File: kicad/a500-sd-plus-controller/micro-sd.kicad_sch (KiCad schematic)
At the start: 19 parts, among them J1 Micro_SD_Card_Det2, J3 Micro_SD_Card_Det2, U10 RT9013-33, U5 SRV05-4, U8 RT9013-33

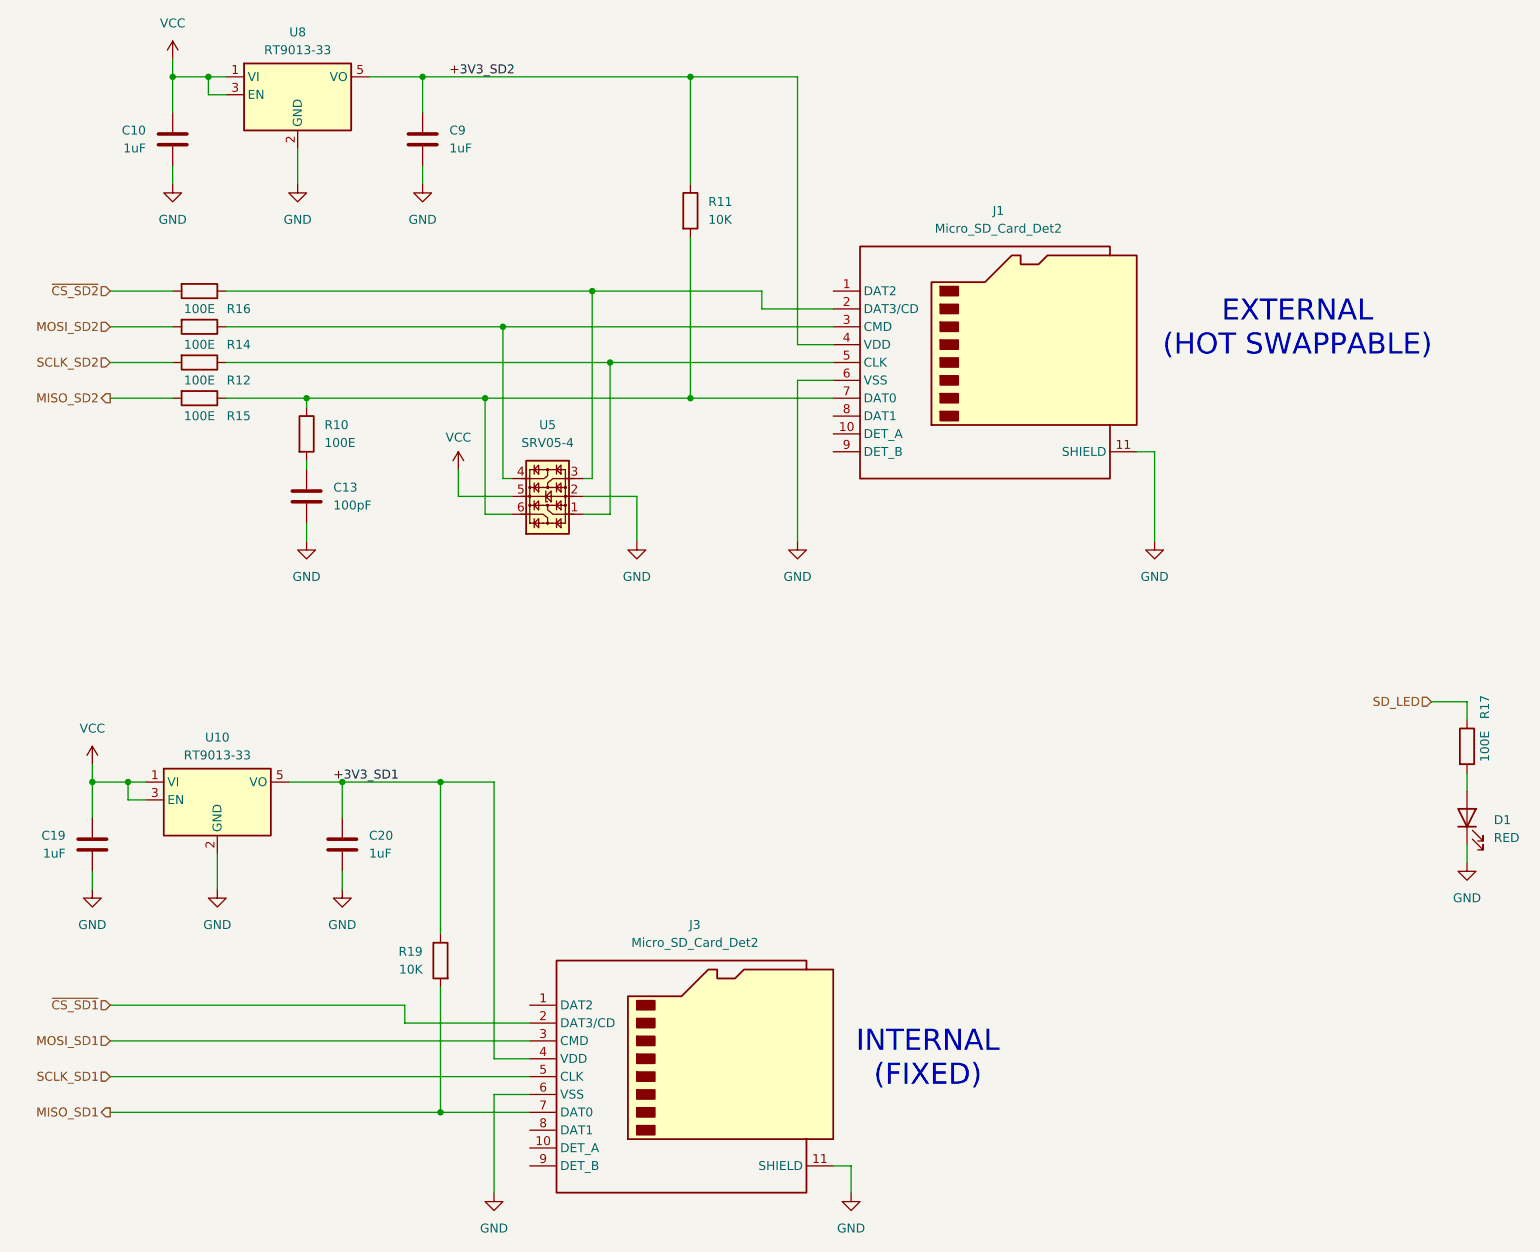
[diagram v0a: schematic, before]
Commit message: added add ethernet controller
still work in progress
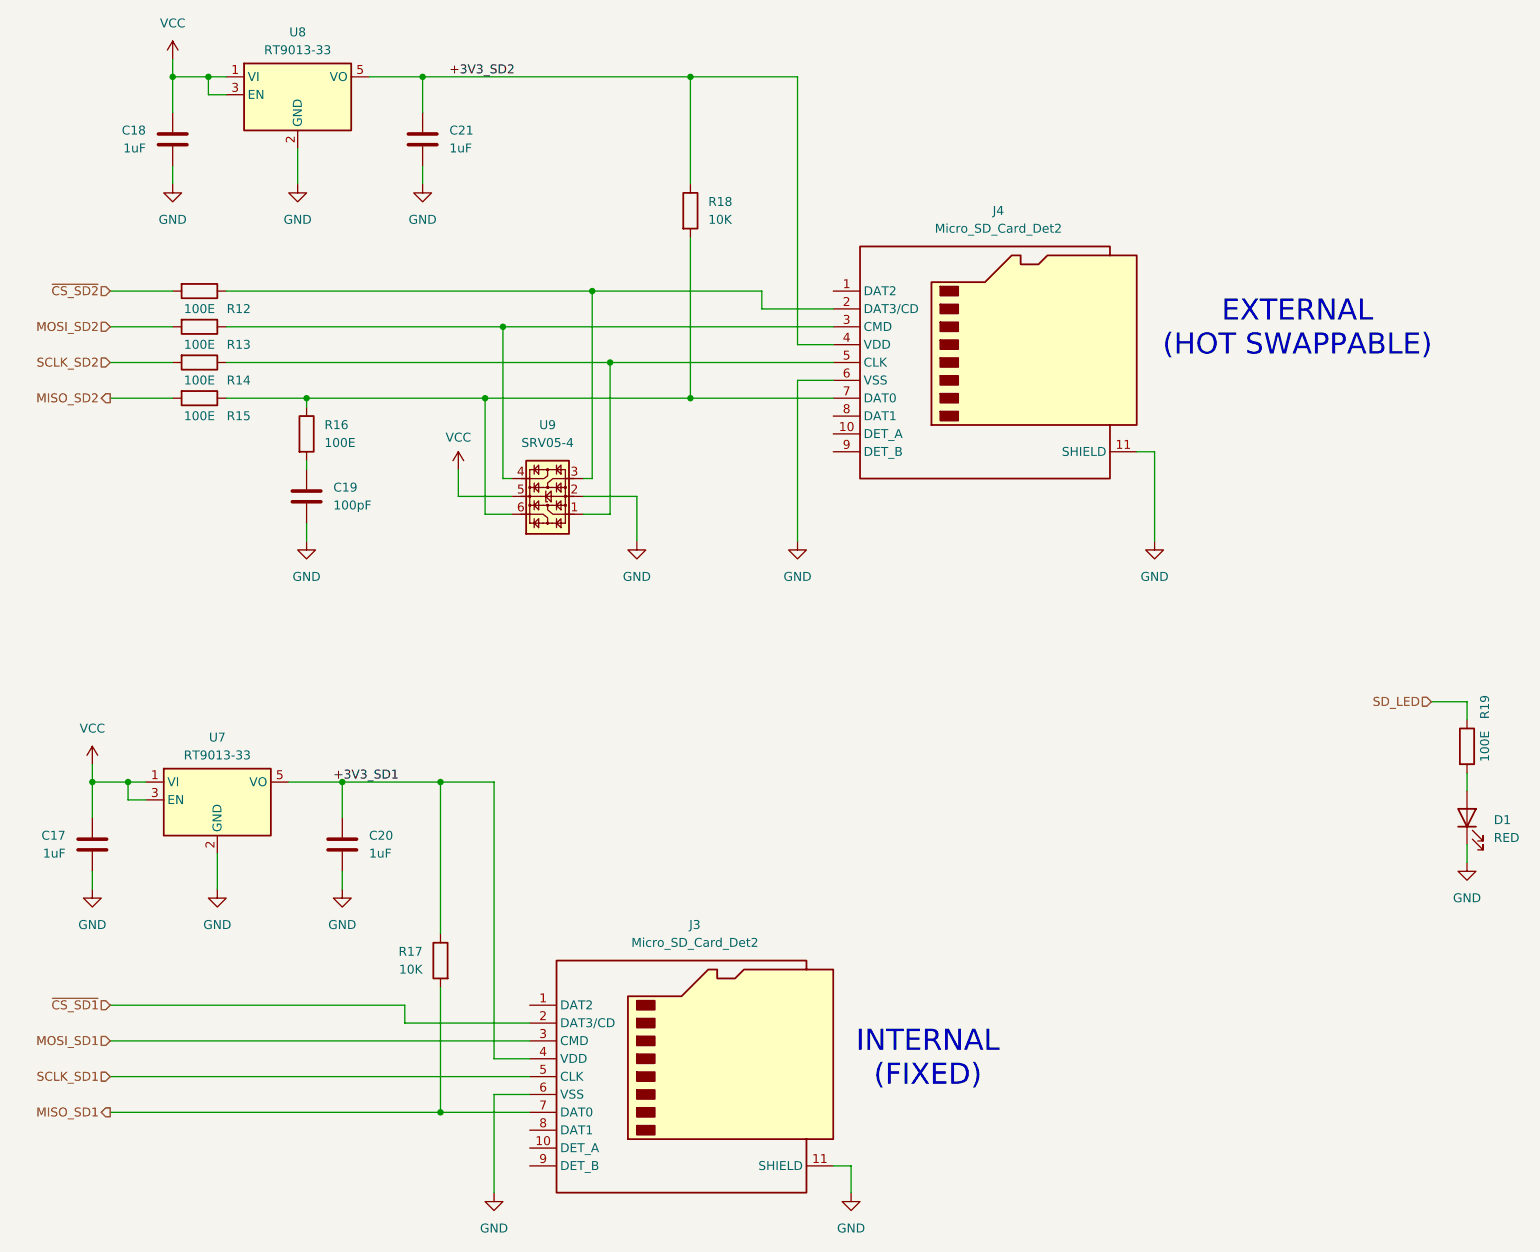
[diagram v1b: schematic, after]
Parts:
- renumbered C19 to C17, C10 to C18, C13 to C19, C9 to C21, J1 to J4, R16 to R12, R14 to R13, R12 to R14, R10 to R16, R19 to R17, R11 to R18, R17 to R19, U10 to U7, U5 to U9
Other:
- company: Mathesar -> Dennis van Weeren
- title: A500-SD-plus-controller -> A500 SD plus controller

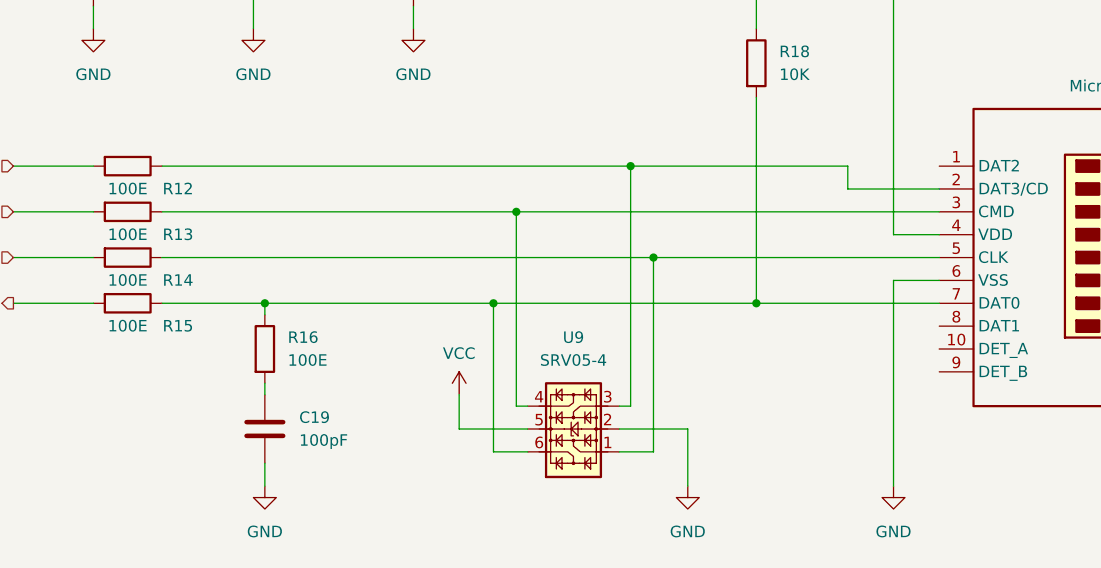
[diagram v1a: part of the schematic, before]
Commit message: routing completely done
todo: review footprints and cleanup silkscreen
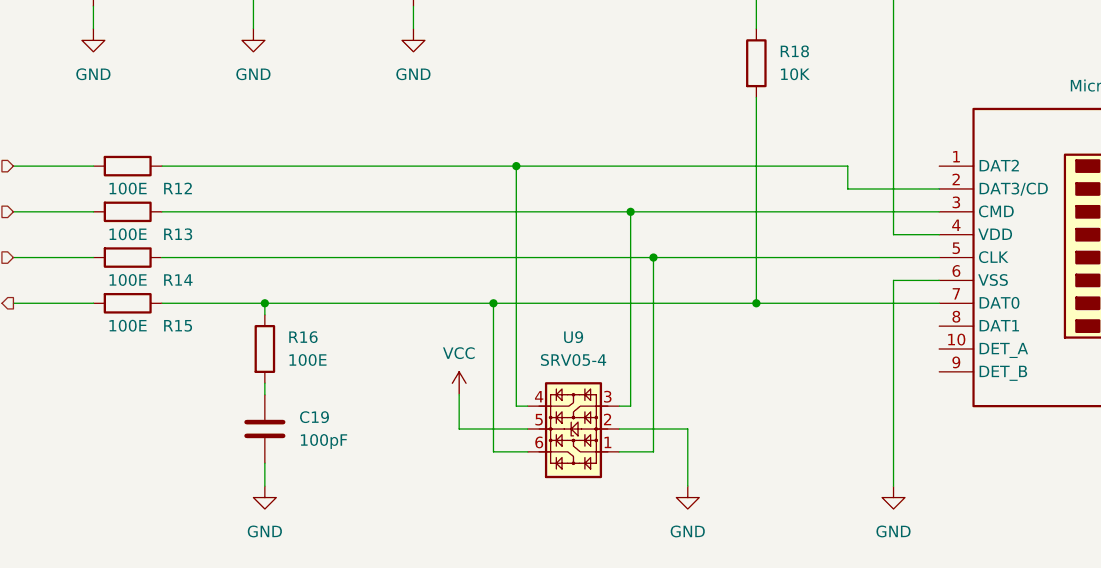
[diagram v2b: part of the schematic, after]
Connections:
- net at J4.2 (DAT3/CD), R12.1: now also U9.4; no longer U9.3
- net at J4.3 (CMD), R13.1: now also U9.3; no longer U9.4
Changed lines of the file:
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@@
+	)
+	(junction
+		(at 104.14 60.96)
+		(diameter 0)
+		(color 0 0 0 0)
 	)
 	(junction
@@
 	)
 	(junction
+		(at 91.44 55.88)
+		(diameter 0)
+		(color 0 0 0 0)
+	)
+	(junction
 		(at 118.11 71.12)
 		(diameter 0)
@@
 	)
 	(junction
-		(at 104.14 55.88)
-		(diameter 0)
-		(color 0 0 0 0)
-	)
-	(junction
 		(at 88.9 71.12)
 		(diameter 0)
 		(color 0 0 0 0)
 	)
-	(junction
-		(at 91.44 60.96)
-		(diameter 0)
-		(color 0 0 0 0)
-	)
 	(wire
 		(pts
@@
 	(wire
 		(pts
+			(xy 104.14 60.96) (xy 104.14 82.55)
+		)
+		(stroke
+			(width 0)
+			(type default)
+		)
+	)
+	(wire
+		(pts
 			(xy 92.71 82.55) (xy 91.44 82.55)
 		)
@@
 	(wire
 		(pts
-			(xy 91.44 60.96) (xy 138.43 60.96)
+			(xy 52.07 60.96) (xy 104.14 60.96)
 		)
 		(stroke
@@
 	(wire
 		(pts
-			(xy 104.14 55.88) (xy 128.27 55.88)
+			(xy 52.07 55.88) (xy 91.44 55.88)
 		)
 		(stroke
@@
 	(wire
 		(pts
-			(xy 104.14 82.55) (xy 104.14 55.88)
-		)
-		(stroke
-			(width 0)
-			(type default)
-		)
-	)
-	(wire
-		(pts
 			(xy 82.55 154.94) (xy 82.55 172.72)
 		)
@@
 	(wire
 		(pts
-			(xy 52.07 60.96) (xy 91.44 60.96)
-		)
-		(stroke
-			(width 0)
-			(type default)
-		)
-	)
-	(wire
-		(pts
-			(xy 91.44 60.96) (xy 91.44 82.55)
-		)
-		(stroke
-			(width 0)
-			(type default)
-		)
-	)
-	(wire
-		(pts
 			(xy 228.6 134.62) (xy 228.6 137.16)
 		)
@@
 	(wire
 		(pts
-			(xy 52.07 55.88) (xy 104.14 55.88)
-		)
-		(stroke
-			(width 0)
-			(type default)
-		)
-	)
-	(wire
-		(pts
 			(xy 35.56 167.64) (xy 95.25 167.64)
 		)
@@
 	(wire
 		(pts
+			(xy 104.14 60.96) (xy 138.43 60.96)
+		)
+		(stroke
+			(width 0)
+			(type default)
+		)
+	)
+	(wire
+		(pts
 			(xy 63.5 71.12) (xy 88.9 71.12)
 		)
@@
 	(wire
 		(pts
+			(xy 91.44 55.88) (xy 91.44 82.55)
+		)
+		(stroke
+			(width 0)
+			(type default)
+		)
+	)
+	(wire
+		(pts
 			(xy 140.97 180.34) (xy 140.97 184.15)
 		)
@@
 		)
 		(stroke
+			(width 0)
+			(type default)
+		)
+	)
+	(wire
+		(pts
+			(xy 91.44 55.88) (xy 128.27 55.88)
+		)
+		(stroke

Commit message: PCB done, this version has been sent to fabrication
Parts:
- C17, C18, C20, C21: LCSC Part # (none) -> C28323; Quantity (none) -> ${QUANTITY}
- C19: LCSC Part # (none) -> C14858; Quantity (none) -> ${QUANTITY}
- D1: LCSC Part # (none) -> C84256; Quantity (none) -> ${QUANTITY}
- J3, J4: LCSC Part # (none) -> C114218; Quantity (none) -> ${QUANTITY}
- R12, R13, R14, R15, R16: value 100E -> 100R; LCSC Part # (none) -> C22775; Quantity (none) -> ${QUANTITY}
- R17, R18: LCSC Part # (none) -> C25804; Quantity (none) -> ${QUANTITY}
- R19: value 100E -> 470R; LCSC Part # (none) -> C23179; Quantity (none) -> ${QUANTITY}
- U7, U8: LCSC Part # (none) -> C587158; Quantity (none) -> ${QUANTITY}
- U9: LCSC Part # (none) -> C2836319; MPN (none) -> SRV05-4; Quantity (none) -> ${QUANTITY}
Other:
- note added: "estimated impedance of micro-sd extension cable is ~100 Ohm (alternating ground, pitch 1.27mm, copper width ~ 0.8mm)"
